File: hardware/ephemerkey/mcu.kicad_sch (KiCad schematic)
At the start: 29 parts, among them J1 SWD TC2030-NL, J2 LOCK IF (I2C JST-PH), Q2 AO3400A, SW1 USER1, SW2 USER2, SW3 USER3/DFU, U1 STM32U083KCU6, Y1 32.768kHz

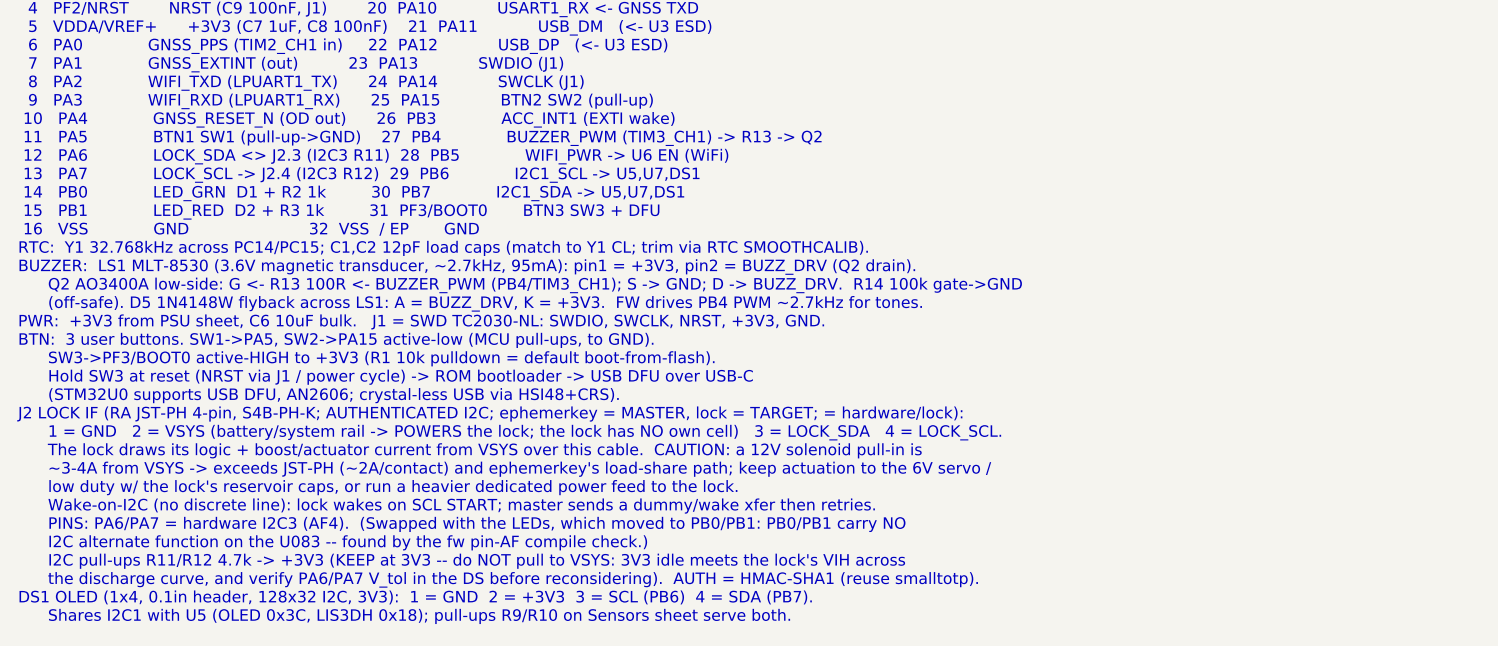
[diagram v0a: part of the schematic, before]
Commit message: hardware+fw: add MAX17048 fuel gauge (U8, I2C1 @0x36) to the PSU sheet
MAX17048G+T10 (LCSC C2682616, TDFN-8 2x2 + EP): 1S ModelGauge SoC monitor,
3uA hibernate, riding the existing I2C1 bus - zero new MCU pins. CELL/VDD
sense at BAT+ (the cell terminal, not VSYS); C31 100nF bypass; CTG/QSTRT/
EP to GND; /ALRT unrouted (no spare pin - firmware polls; alert register
still usable). SDA/SCL logic is independent of VDD, so the 3V3 bus vs a
fading BAT+ is fine.

- Symbol authored into lib/symbols/ephemerkey.kicad_sym from the ADI
  datasheet pin table, cross-checked pin-for-pin against the independently
  authored notchdeck:MAX17048 (sibling project; identical map, same stdlib
  TDFN-8-1EP_2x2mm_P0.5mm_EP0.8x1.2mm footprint). Shared caveat recorded:
  verify EP land vs ADI 21-0168 before fab.
- psu.kicad_sch: surgical splice (sheet is hand-wired; no regen): embedded
  lib symbol, U8 + C31 instances placed near J4, note block updated with
  full pin map + wiring guidance. Property text offsets fixed to be
  relative to the new bodies (KiCad stores them absolute). Render-verified.
- Bus enumerations updated (mcu/sensors/storage notes, manifest + sheets):
  I2C1 = U5 0x18 + DS1 0x3C + U7 0x50-53 + U8 0x36.
- PARTS.md, DESIGN.md (pin table, peripheral summary, BOM).
- ephemerkey-rs: sensors task probes MAX17048 VERSION alongside LIS3DH
  WHO_AM_I; VCELL/SOC register consts staged.

Co-Authored-By: Claude Fable 5 <noreply@anthropic.com>
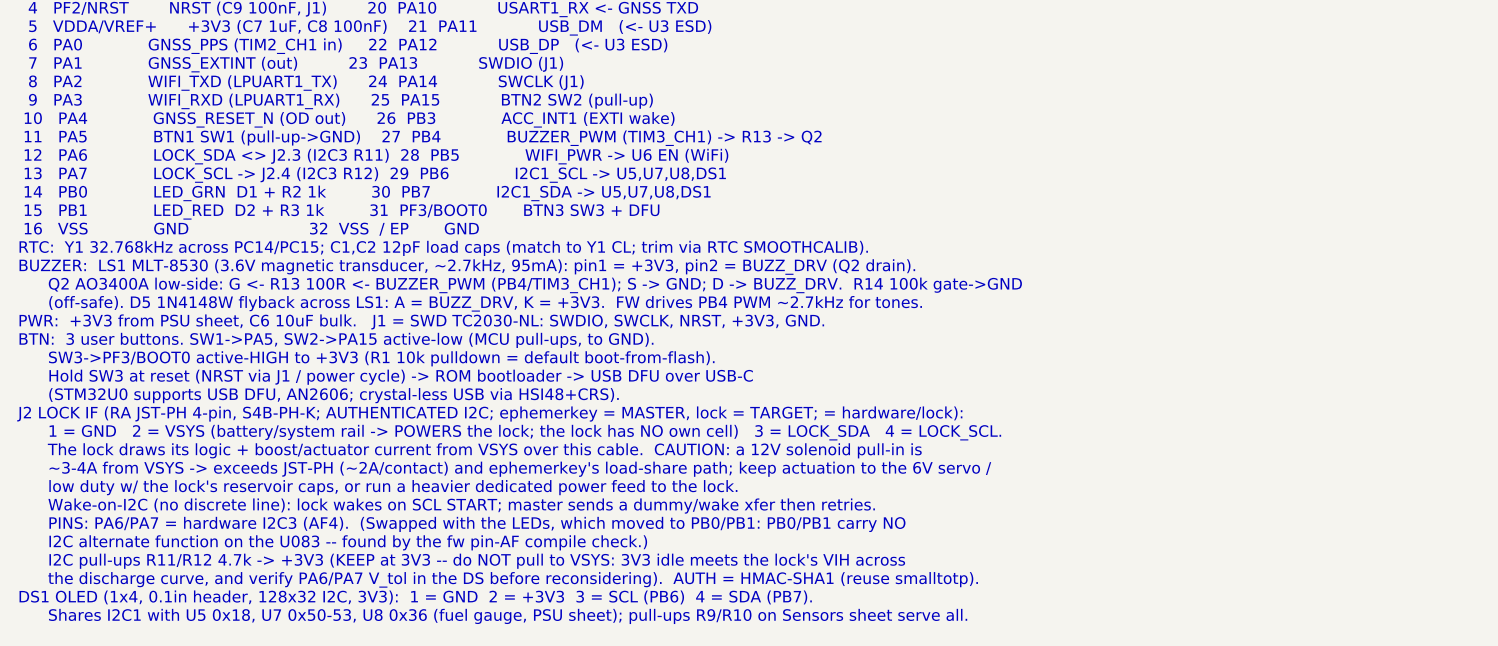
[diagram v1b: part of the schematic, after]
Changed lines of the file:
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@@
 		(company "EphemerKey Authors")
 	)
-	(text "MCU / RTC / Programming — pinout (U1 STM32U083KCU6, UFQFPN-32).  PLACED, not wired.\n pin  name            net / function           pin  name            net / function\n  1   VDD             +3V3  (C3 100nF)           17  VDDUSB          +3V3  (C5 100nF)\n  2   PC14/OSC32_IN   Y1 LSE 32.768kHz           18  PA8             ACC_INT2 (EXTI tamper)\n  3   PC15/OSC32_OUT  Y1 LSE 32.768kHz           19  PA9             USART1_TX -> GNSS RXD\n  4   PF2/NRST        NRST (C9 100nF, J1)        20  PA10            USART1_RX <- GNSS TXD\n  5   VDDA/VREF+      +3V3 (C7 1uF, C8 100nF)    21  PA11            USB_DM   (<- U3 ESD)\n  6   PA0             GNSS_PPS (TIM2_CH1 in)     22  PA12            USB_DP   (<- U3 ESD)\n  7   PA1             GNSS_EXTINT (out)          23  PA13            SWDIO (J1)\n  8   PA2             WIFI_TXD (LPUART1_TX)      24  PA14            SWCLK (J1)\n  9   PA3             WIFI_RXD (LPUART1_RX)      25  PA15            BTN2 SW2 (pull-up)\n 10   PA4             GNSS_RESET_N (OD out)      26  PB3             ACC_INT1 (EXTI wake)\n 11   PA5             BTN1 SW1 (pull-up->GND)    27  PB4             BUZZER_PWM (TIM3_CH1) -> R13 -> Q2\n 12   PA6             LOCK_SDA <> J2.3 (I2C3 R11)  28  PB5             WIFI_PWR -> U6 EN (WiFi)\n 13   PA7             LOCK_SCL -> J2.4 (I2C3 R12)  29  PB6             I2C1_SCL -> U5,U7,DS1\n 14   PB0             LED_GRN  D1 + R2 1k         30  PB7             I2C1_SDA -> U5,U7,DS1\n 15   PB1             LED_RED  D2 + R3 1k         31  PF3/BOOT0       BTN3 SW3 + DFU\n 16   VSS             GND                        32  VSS  / EP       GND\nRTC:  Y1 32.768kHz across PC14/PC15; C1,C2 12pF load caps (match to Y1 CL; trim via RTC SMOOTHCALIB).\nBUZZER:  LS1 MLT-8530 (3.6V magnetic transducer, ~2.7kHz, 95mA): pin1 = +3V3, pin2 = BUZZ_DRV (Q2 drain).\n      Q2 AO3400A low-side: G <- R13 100R <- BUZZER_PWM (PB4/TIM3_CH1); S -> GND; D -> BUZZ_DRV.  R14 100k gate->GND\n      (off-safe). D5 1N4148W flyback across LS1: A = BUZZ_DRV, K = +3V3.  FW drives PB4 PWM ~2.7kHz for tones.\nPWR:  +3V3 from PSU sheet, C6 10uF bulk.   J1 = SWD TC2030-NL: SWDIO, SWCLK, NRST, +3V3, GND.\nBTN:  3 user buttons. SW1->PA5, SW2->PA15 active-low (MCU pull-ups, to GND).\n      SW3->PF3/BOOT0 active-HIGH to +3V3 (R1 10k pulldown = default boot-from-flash).\n      Hold SW3 at reset (NRST via J1 / power cycle) -> ROM bootloader -> USB DFU over USB-C\n      (STM32U0 supports USB DFU, AN2606; crystal-less USB via HSI48+CRS).\nJ2 LOCK IF (RA JST-PH 4-pin, S4B-PH-K; AUTHENTICATED I2C; ephemerkey = MASTER, lock = TARGET; = hardware/lock):\n      1 = GND   2 = VSYS (battery/system rail -> POWERS the lock; the lock has NO own cell)   3 = LOCK_SDA   4 = LOCK_SCL.\n      The lock draws its logic + boost/actuator current from VSYS over this cable.  CAUTION: a 12V solenoid pull-in is\n      ~3-4A from VSYS -> exceeds JST-PH (~2A/contact) and ephemerkey's load-share path; keep actuation to the 6V servo /\n      low duty w/ the lock's reservoir caps, or run a heavier dedicated power feed to the lock.\n      Wake-on-I2C (no discrete line): lock wakes on SCL START; master sends a dummy/wake xfer then retries.\n      PINS: PA6/PA7 = hardware I2C3 (AF4).  (Swapped with the LEDs, which moved to PB0/PB1: PB0/PB1 carry NO\n      I2C alternate function on the U083 -- found by the fw pin-AF compile check.)\n      I2C pull-ups R11/R12 4.7k -> +3V3 (KEEP at 3V3 -- do NOT pull to VSYS: 3V3 idle meets the lock's VIH across\n      the discharge curve, and verify PA6/PA7 V_tol in the DS before reconsidering).  AUTH = HMAC-SHA1 (reuse smalltotp).\nDS1 OLED (1x4, 0.1in header, 128x32 I2C, 3V3):  1 = GND  2 = +3V3  3 = SCL (PB6)  4 = SDA (PB7).\n      Shares I2C1 with U5 (OLED 0x3C, LIS3DH 0x18); pull-ups R9/R10 on Sensors sheet serve both."
+	(text "MCU / RTC / Programming — pinout (U1 STM32U083KCU6, UFQFPN-32).  PLACED, not wired.\n pin  name            net / function           pin  name            net / function\n  1   VDD             +3V3  (C3 100nF)           17  VDDUSB          +3V3  (C5 100nF)\n  2   PC14/OSC32_IN   Y1 LSE 32.768kHz           18  PA8             ACC_INT2 (EXTI tamper)\n  3   PC15/OSC32_OUT  Y1 LSE 32.768kHz           19  PA9             USART1_TX -> GNSS RXD\n  4   PF2/NRST        NRST (C9 100nF, J1)        20  PA10            USART1_RX <- GNSS TXD\n  5   VDDA/VREF+      +3V3 (C7 1uF, C8 100nF)    21  PA11            USB_DM   (<- U3 ESD)\n  6   PA0             GNSS_PPS (TIM2_CH1 in)     22  PA12            USB_DP   (<- U3 ESD)\n  7   PA1             GNSS_EXTINT (out)          23  PA13            SWDIO (J1)\n  8   PA2             WIFI_TXD (LPUART1_TX)      24  PA14            SWCLK (J1)\n  9   PA3             WIFI_RXD (LPUART1_RX)      25  PA15            BTN2 SW2 (pull-up)\n 10   PA4             GNSS_RESET_N (OD out)      26  PB3             ACC_INT1 (EXTI wake)\n 11   PA5             BTN1 SW1 (pull-up->GND)    27  PB4             BUZZER_PWM (TIM3_CH1) -> R13 -> Q2\n 12   PA6             LOCK_SDA <> J2.3 (I2C3 R11)  28  PB5             WIFI_PWR -> U6 EN (WiFi)\n 13   PA7             LOCK_SCL -> J2.4 (I2C3 R12)  29  PB6             I2C1_SCL -> U5,U7,U8,DS1\n 14   PB0             LED_GRN  D1 + R2 1k         30  PB7             I2C1_SDA -> U5,U7,U8,DS1\n 15   PB1             LED_RED  D2 + R3 1k         31  PF3/BOOT0       BTN3 SW3 + DFU\n 16   VSS             GND                        32  VSS  / EP       GND\nRTC:  Y1 32.768kHz across PC14/PC15; C1,C2 12pF load caps (match to Y1 CL; trim via RTC SMOOTHCALIB).\nBUZZER:  LS1 MLT-8530 (3.6V magnetic transducer, ~2.7kHz, 95mA): pin1 = +3V3, pin2 = BUZZ_DRV (Q2 drain).\n      Q2 AO3400A low-side: G <- R13 100R <- BUZZER_PWM (PB4/TIM3_CH1); S -> GND; D -> BUZZ_DRV.  R14 100k gate->GND\n      (off-safe). D5 1N4148W flyback across LS1: A = BUZZ_DRV, K = +3V3.  FW drives PB4 PWM ~2.7kHz for tones.\nPWR:  +3V3 from PSU sheet, C6 10uF bulk.   J1 = SWD TC2030-NL: SWDIO, SWCLK, NRST, +3V3, GND.\nBTN:  3 user buttons. SW1->PA5, SW2->PA15 active-low (MCU pull-ups, to GND).\n      SW3->PF3/BOOT0 active-HIGH to +3V3 (R1 10k pulldown = default boot-from-flash).\n      Hold SW3 at reset (NRST via J1 / power cycle) -> ROM bootloader -> USB DFU over USB-C\n      (STM32U0 supports USB DFU, AN2606; crystal-less USB via HSI48+CRS).\nJ2 LOCK IF (RA JST-PH 4-pin, S4B-PH-K; AUTHENTICATED I2C; ephemerkey = MASTER, lock = TARGET; = hardware/lock):\n      1 = GND   2 = VSYS (battery/system rail -> POWERS the lock; the lock has NO own cell)   3 = LOCK_SDA   4 = LOCK_SCL.\n      The lock draws its logic + boost/actuator current from VSYS over this cable.  CAUTION: a 12V solenoid pull-in is\n      ~3-4A from VSYS -> exceeds JST-PH (~2A/contact) and ephemerkey's load-share path; keep actuation to the 6V servo /\n      low duty w/ the lock's reservoir caps, or run a heavier dedicated power feed to the lock.\n      Wake-on-I2C (no discrete line): lock wakes on SCL START; master sends a dummy/wake xfer then retries.\n      PINS: PA6/PA7 = hardware I2C3 (AF4).  (Swapped with the LEDs, which moved to PB0/PB1: PB0/PB1 carry NO\n      I2C alternate function on the U083 -- found by the fw pin-AF compile check.)\n      I2C pull-ups R11/R12 4.7k -> +3V3 (KEEP at 3V3 -- do NOT pull to VSYS: 3V3 idle meets the lock's VIH across\n      the discharge curve, and verify PA6/PA7 V_tol in the DS before reconsidering).  AUTH = HMAC-SHA1 (reuse smalltotp).\nDS1 OLED (1x4, 0.1in header, 128x32 I2C, 3V3):  1 = GND  2 = +3V3  3 = SCL (PB6)  4 = SDA (PB7).\n      Shares I2C1 with U5 0x18, U7 0x50-53, U8 0x36 (fuel gauge, PSU sheet); pull-ups R9/R10 on Sensors sheet serve all."
 		(exclude_from_sim no)
 		(at 12 198.88 0)
